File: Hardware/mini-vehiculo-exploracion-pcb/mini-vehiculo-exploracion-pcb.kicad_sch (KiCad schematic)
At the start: 19 parts, among them IC1 BME690, J1 ArducamMINIOV2640, U1 BNO086, U2 ESP32-S3-WROOM-1, Y1 830003000

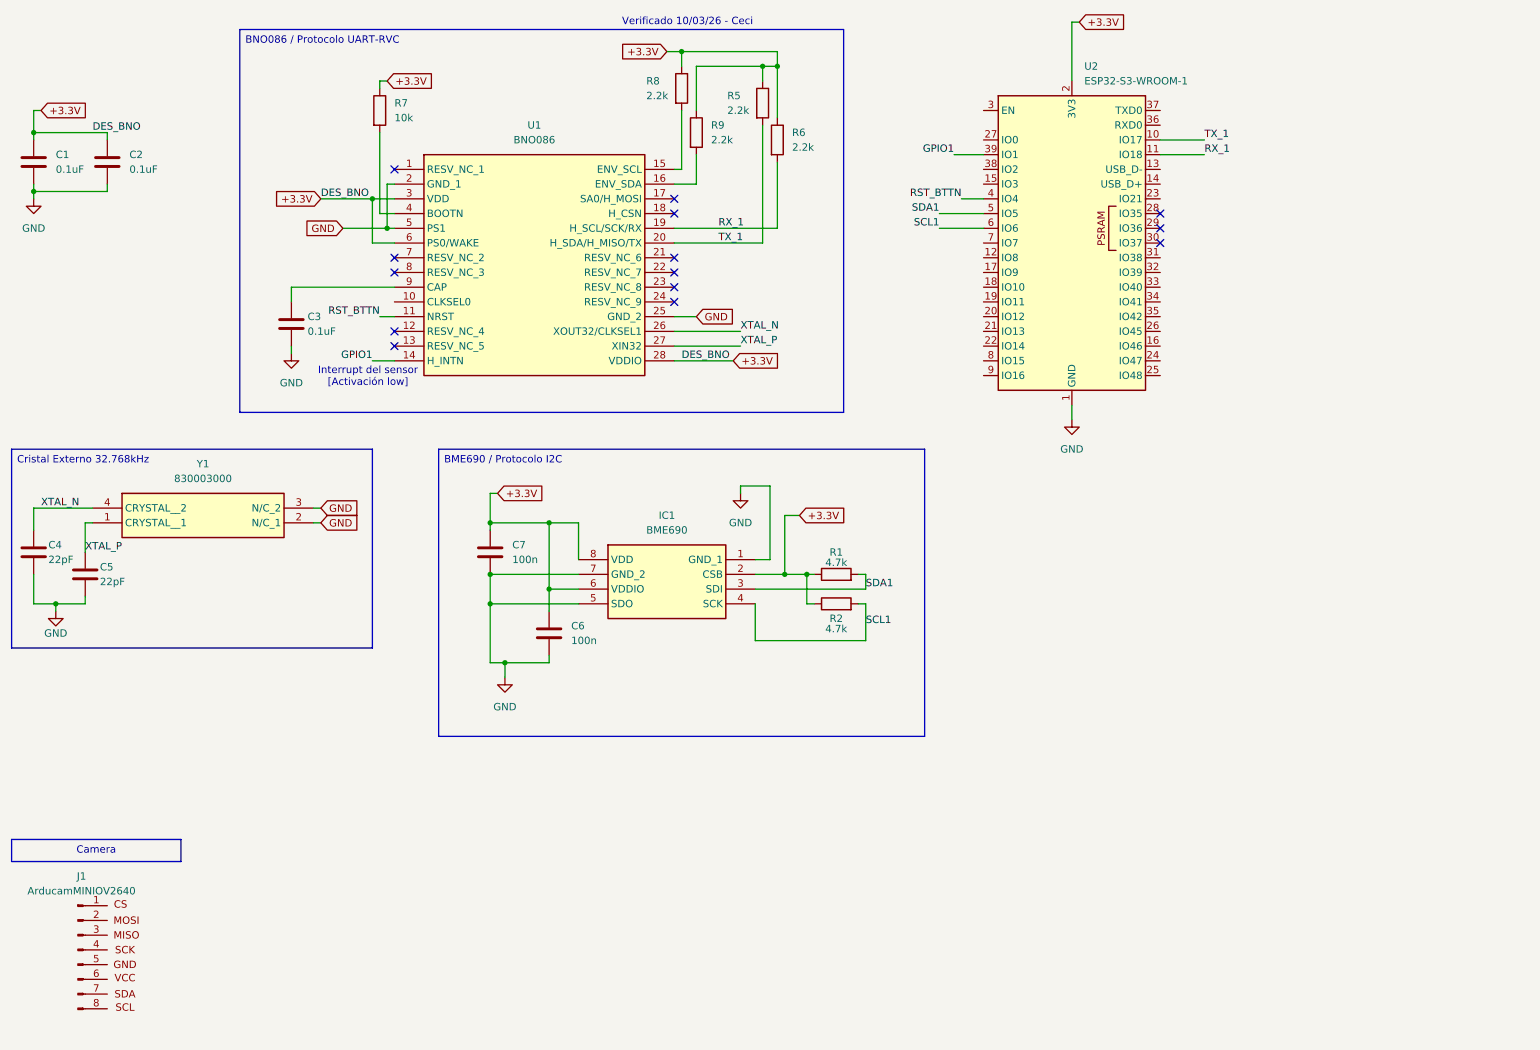
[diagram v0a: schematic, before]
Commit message: Pins for camera and drivers
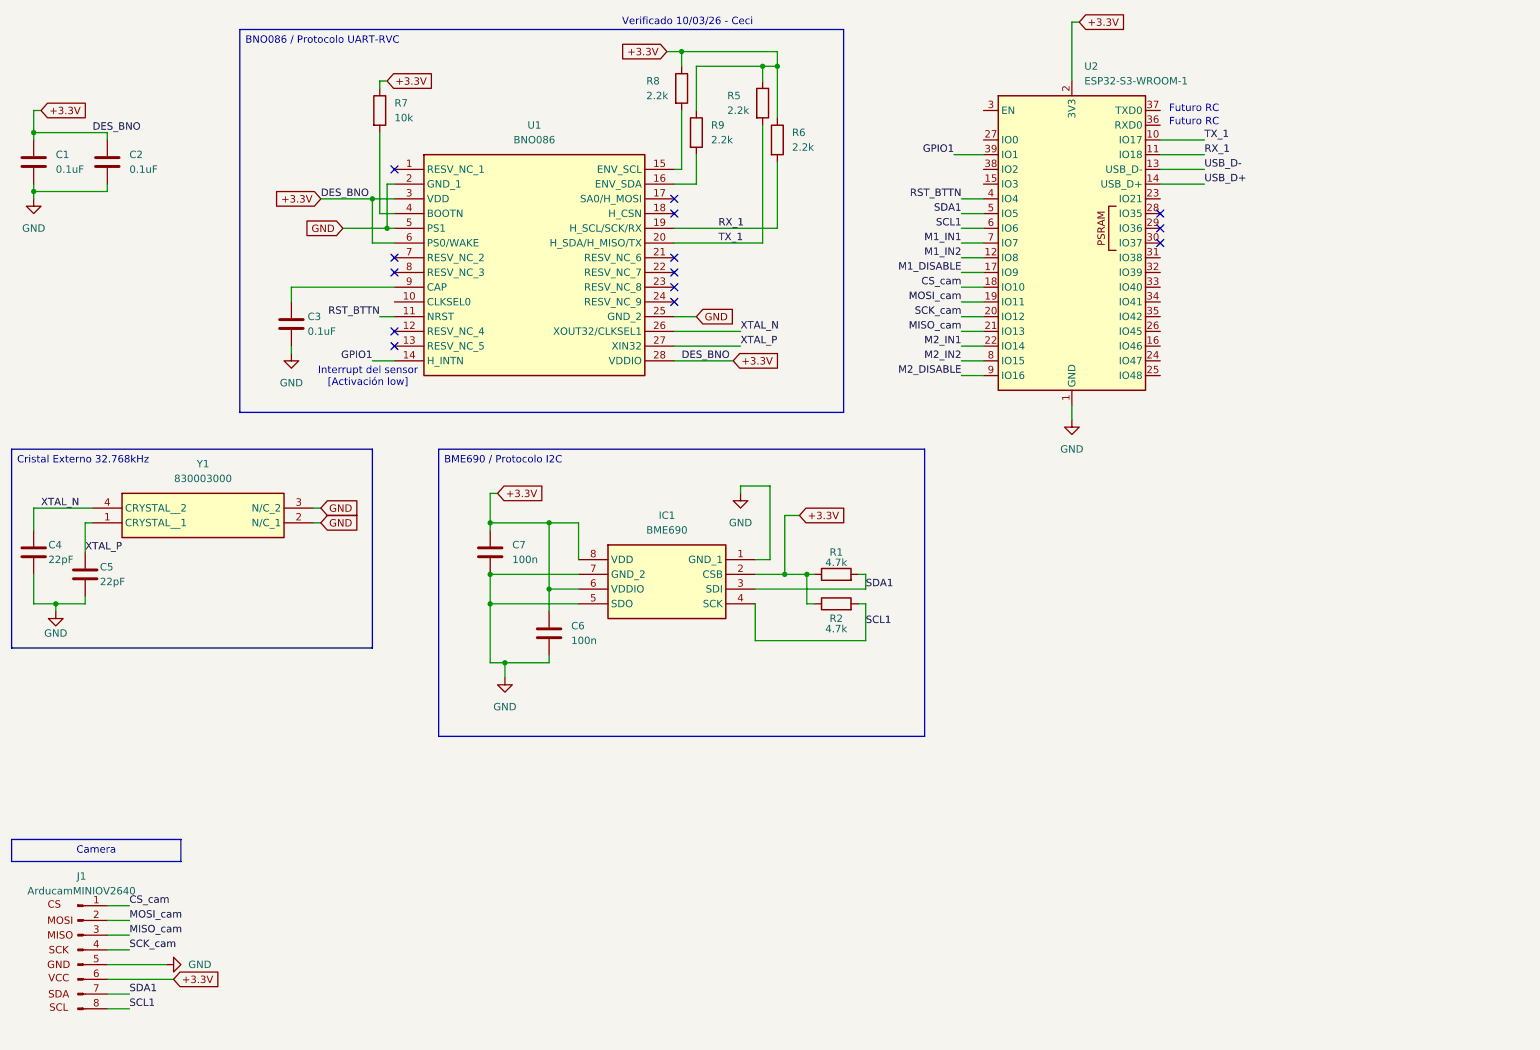
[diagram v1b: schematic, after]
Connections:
- net +3.3V: now also J1.6 (VCC)
- net GND: now also J1.5 (GND)
- net SCL1: now also J1.8 (SCL)
- net SDA1: now also J1.7 (SDA)
- net M1_IN2: now reaches U2.12 (IO8)
- net USB_D-: now reaches U2.13 (USB_D-)
- net USB_D+: now reaches U2.14 (USB_D+)
- net M1_DISABLE: now reaches U2.17 (IO9)
- net CS_cam: now reaches U2.18 (IO10)
- net CS_cam: now also J1.1 (CS)
- net MOSI_cam: now reaches U2.19 (IO11)
- net MOSI_cam: now also J1.2 (MOSI)
- net SCK_cam: now reaches U2.20 (IO12)
- net SCK_cam: now also J1.4 (SCK)
- net MISO_cam: now reaches U2.21 (IO13)
- net MISO_cam: now also J1.3 (MISO)
- net M2_IN1: now reaches U2.22 (IO14)
- net M1_IN1: now reaches U2.7 (IO7)
- net M2_IN2: now reaches U2.8 (IO15)
- net M2_DISABLE: now reaches U2.9 (IO16)
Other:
- note added: "Futuro RC"
- moved on the sheet: J1

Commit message: Add enable circuit and USB schematic v1
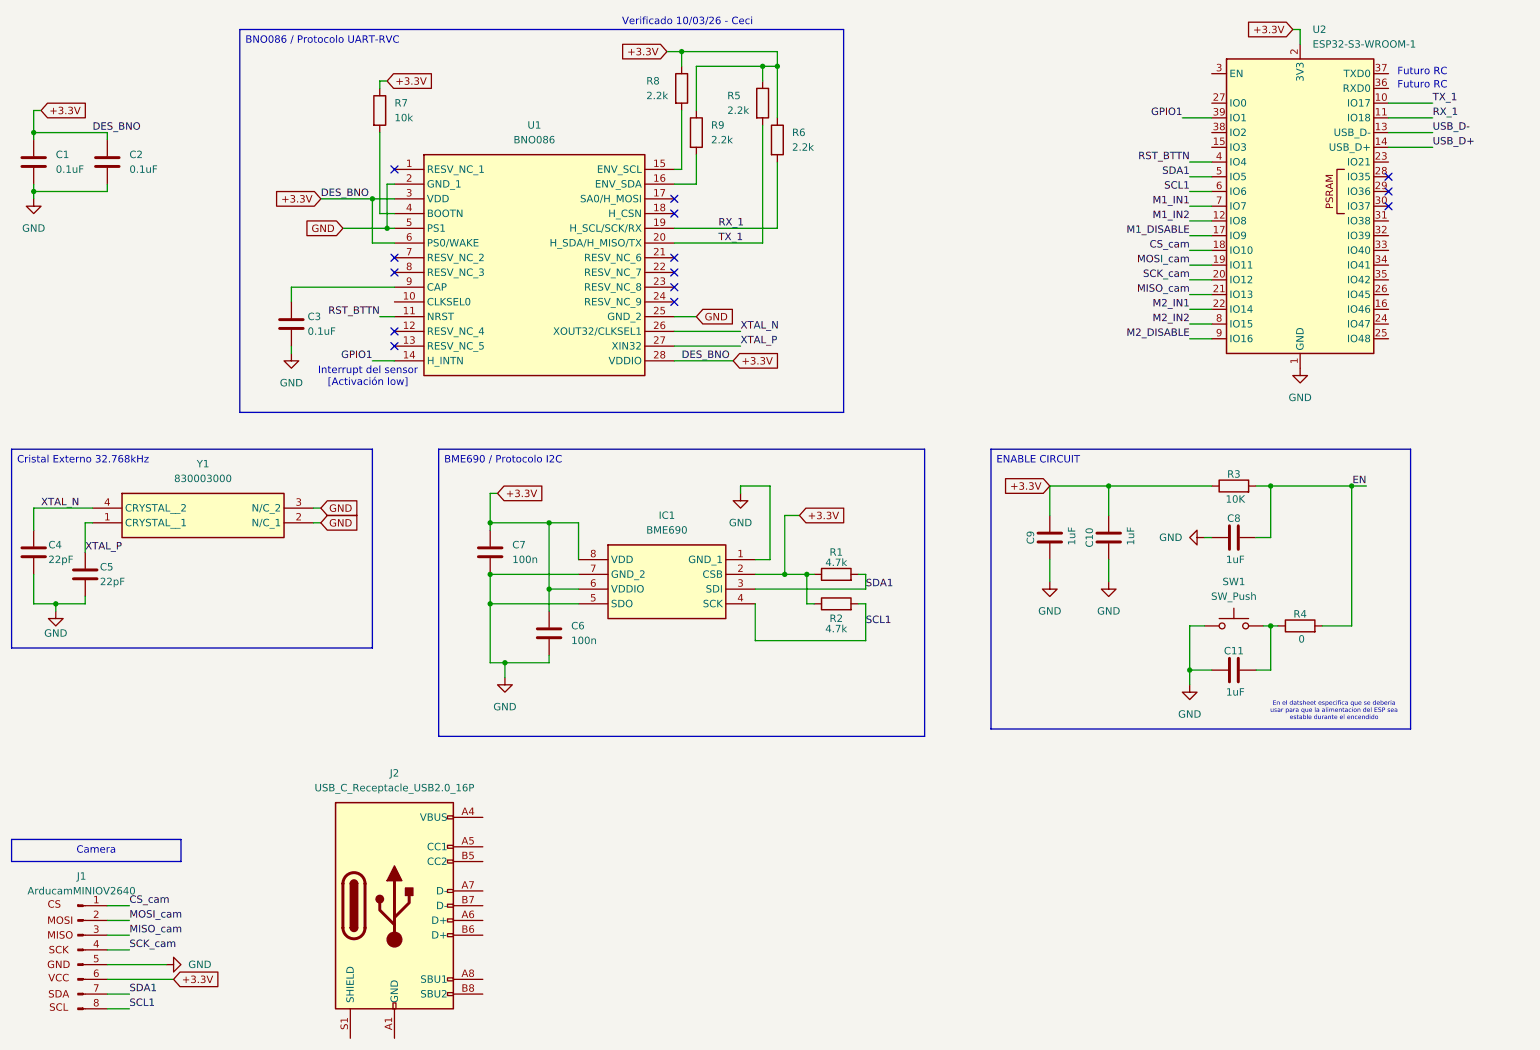
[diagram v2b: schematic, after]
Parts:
- added C10, C11, C8, C9: 1uF, symbol Device:C
- added J2: USB_C_Receptacle_USB2.0_16P, symbol Connector:USB_C_Receptacle_USB2.0_16P
- added R3: 10K, symbol Device:R
- added R4: 0, symbol Device:R
- added SW1: SW_Push, symbol Switch:SW_Push
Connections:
- net +3.3V: now also C10.2, C9.2, R3.1
- net GND: now also C10.1, C11.1, C8.1, C9.1, SW1.1
- new net: C11.2, R4.1, SW1.2
- new net: J2.A1 (GND), J2.A12 (GND), J2.B1 (GND), J2.B12 (GND)
- new net: J2.A4 (VBUS), J2.A9 (VBUS), J2.B4 (VBUS), J2.B9 (VBUS)
- new net EN: C8.2, R3.2, R4.2
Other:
- note added: "En el datsheet especifica que se deberia usar para que la alimentacion del ESP sea estable durante el encendido"
- moved on the sheet: U2

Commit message: Add n_FAULT pin, changed I2C pins for cam
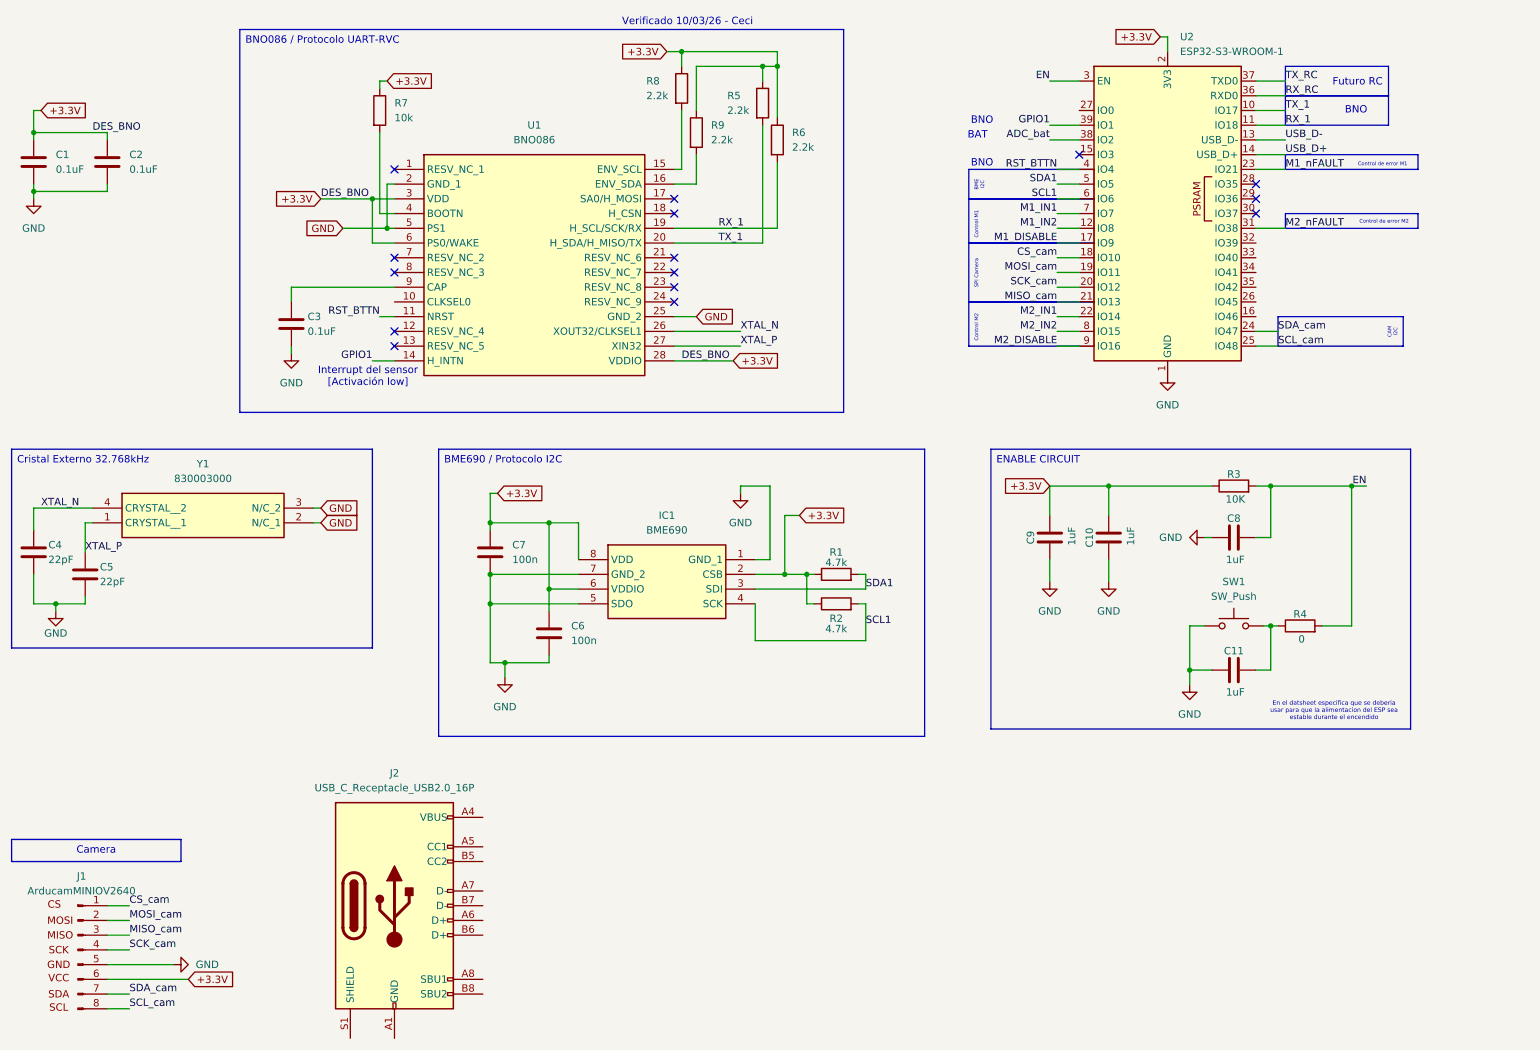
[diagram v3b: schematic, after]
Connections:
- net EN: now also U2.3 (EN)
- net SCL1: no longer J1.8 (SCL)
- net SDA1: no longer J1.7 (SDA)
- net M1_nFAULT: now reaches U2.23 (IO21)
- net SDA_cam: now reaches U2.24 (IO47)
- net SDA_cam: now also J1.7 (SDA)
- net SCL_cam: now reaches U2.25 (IO48)
- net SCL_cam: now also J1.8 (SCL)
- net M2_nFAULT: now reaches U2.31 (IO38)
- net RX_RC: now reaches U2.36 (RXD0)
- net TX_RC: now reaches U2.37 (TXD0)
- net ADC_bat: now reaches U2.38 (IO2)
- no-connect marks 14 -> 15
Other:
- note added: "BAT"
- note added: "BNO"
- note added: "Control de error M1"
- note added: "Control de error M2"
- moved on the sheet: U2

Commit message: Add USB protection
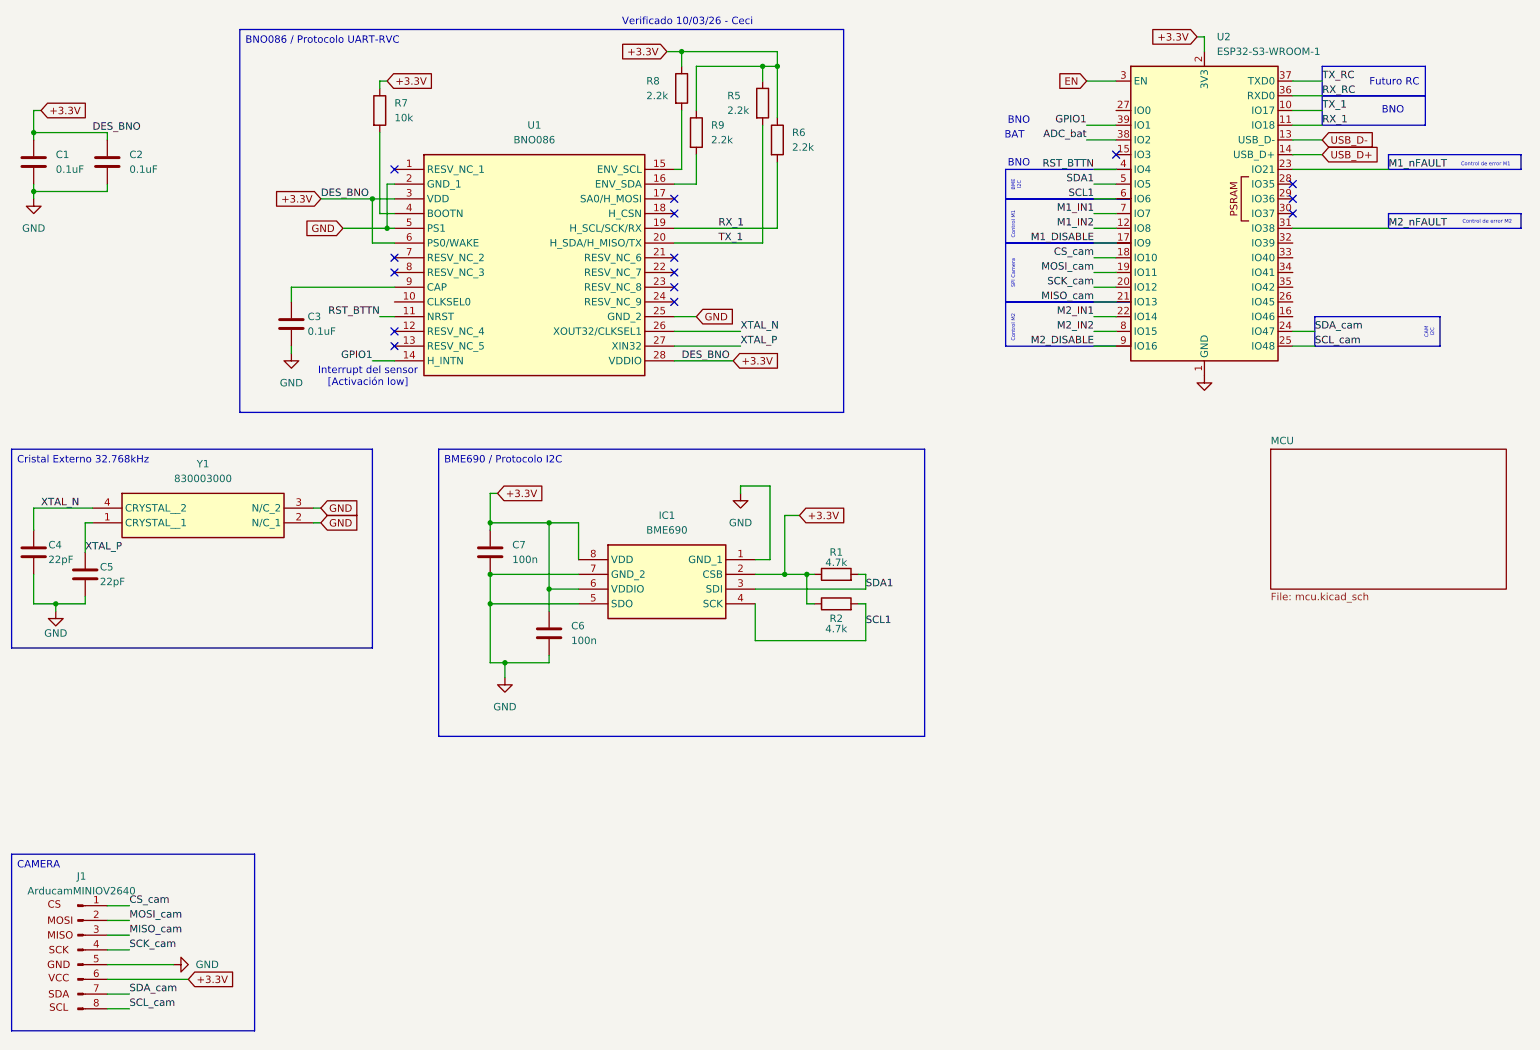
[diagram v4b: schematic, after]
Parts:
- removed C10, C11, C8, C9: 1uF, symbol Device:C
- removed J2: USB_C_Receptacle_USB2.0_16P, symbol Connector:USB_C_Receptacle_USB2.0_16P
- removed R3: 10K, symbol Device:R
- removed R4: 0, symbol Device:R
- removed SW1: SW_Push, symbol Switch:SW_Push
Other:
- added sheet MCU (mcu.kicad_sch)
- note removed: "En el datsheet especifica que se deberia usar para que la alimentacion del ESP sea estable durante el encendido"
- moved on the sheet: U2

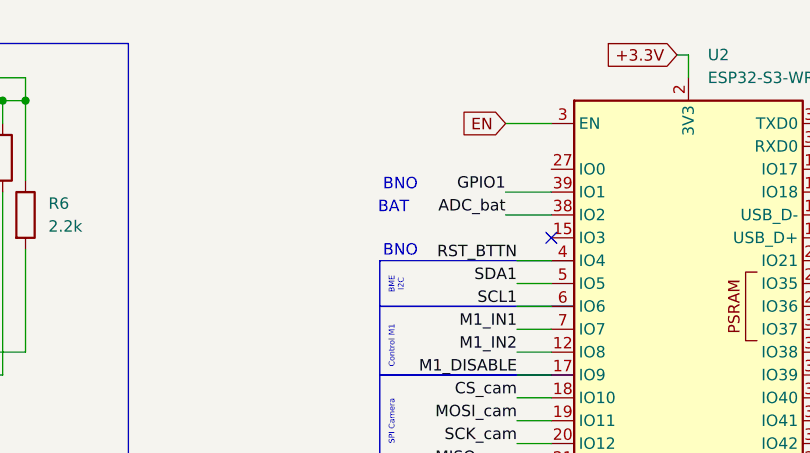
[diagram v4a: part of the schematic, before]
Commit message: Add boot to the schematic
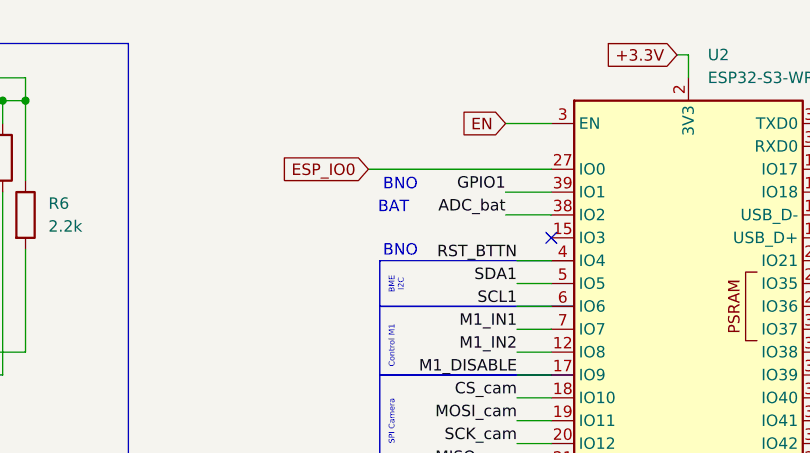
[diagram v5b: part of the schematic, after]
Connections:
- net ESP_IO0: now reaches U2.27 (IO0)
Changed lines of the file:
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@@
+	(wire
+		(pts
+			(xy 187.96 31.75) (xy 208.28 31.75)
+		)
+		(stroke
+			(width 0)
+			(type default)
+		)
+	)
 	(wire
 		(pts
@@
 		)
 	)
+	(global_label "ESP_IO0"
+		(shape input)
+		(at 187.96 31.75 180)
+		(fields_autoplaced yes)
+		(effects
+			(font
+				(size 1.27 1.27)
+			)
+			(justify right)
+		)
+		(property "Intersheetrefs" "${INTERSHEET_REFS}"
+			(at 177.2339 31.75 0)
+			(effects
+				(font
+					(size 1.27 1.27)
+				)
+				(justify right)
+				(hide yes)
+			)
+		)
+	)

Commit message: checking schematic/sheets
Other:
- note added: "Planilla OK"
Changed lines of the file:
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@@
+		)
+	)
+	(text "Planilla OK"
+		(exclude_from_sim no)
+		(at 212.852 77.978 0)
+		(effects
+			(font
+				(size 1.27 1.27)
+				(color 255 0 235 1)
+			)
 		)
 	)
@@
 		)
 	)
+	(text "Planilla OK"
+		(exclude_from_sim no)
+		(at 63.246 16.256 0)
+		(effects
+			(font
+				(size 1.27 1.27)
+				(color 255 0 235 1)
+			)
+		)
+	)
 	(text "Control de error M1"
 		(exclude_from_sim no)
@@
 			(font
 				(size 0.635 0.635)
+			)
+		)
+	)
+	(text "Planilla OK"
+		(exclude_from_sim no)
+		(at 73.406 89.154 0)
+		(effects
+			(font
+				(size 1.27 1.27)
+				(color 255 0 235 1)
+			)
+		)
+	)
+	(text "Planilla OK"
+		(exclude_from_sim no)
+		(at 53.594 159.004 0)
+		(effects
+			(font
+				(size 1.27 1.27)
+				(color 255 0 235 1)
 			)
 		)
@@
 			)
 		)
+	)
+	(text "Planilla OK"
+		(exclude_from_sim no)
+		(at 98.044 88.392 0)
+		(effects
+			(font
+				(size 1.27 1.27)
+				(color 255 0 235 1)
+			)
+		)
